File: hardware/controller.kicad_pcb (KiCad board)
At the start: 4 copper layers, 31.2 x 93.2 mm, 42 parts, among them J1 Connector, USB-TYPE-C-16P, J2 AXK6F20347YG, J3 AFA01-S08FCA-00, U1 ESP32-C6-WROOM-1, U2 BQ24074RGTR, U3 TLA2518IRTER, U6 TPS62142RGTR

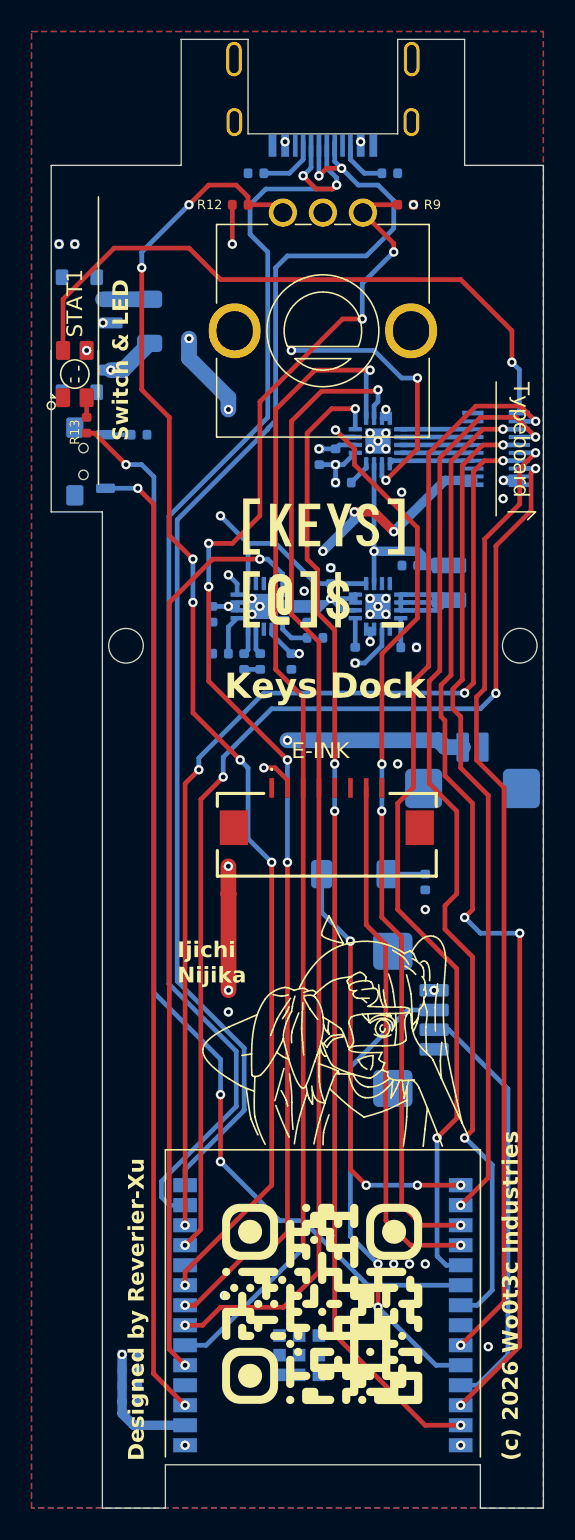
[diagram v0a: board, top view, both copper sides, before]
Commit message: :art: improve LED positions
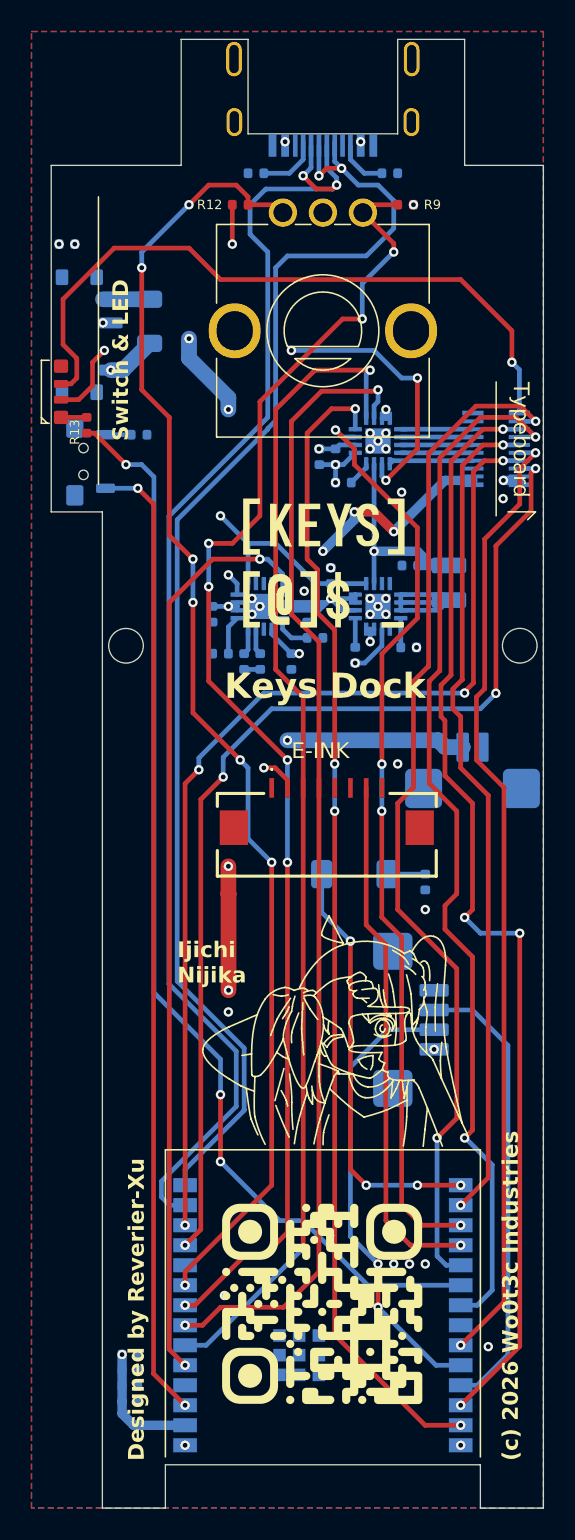
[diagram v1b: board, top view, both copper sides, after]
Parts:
- removed STAT1: ~, KeysDock:XL-3528RGBW-WS2812B
- added LED1: ~, KeysDock:XL-3512RGBW-WS2812B, F.Cu at (132.0, 68.1)
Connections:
- PC1 pad 1: P,E -> /USB_PWR_SUPP
- PC1 pad 2: /U0TX -> /U0RX
- PC1 pad 3: /U0RX -> /U0TX
- PC1 pad 4: /USB_PWR_SUPP -> P,E
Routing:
- net P,+5: track 61.5 -> 65.3 mm
- net /TOMO0: track 40.7 -> 44.0 mm
- net /U0TX: track 26.9 -> 29.1 mm
- net /USB_PWR_SUPP: track 84.6 -> 86.1 mm
- net /U0RX: track 29.6 -> 29.0 mm
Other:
- board text added: "-0 TX RX +5"
- board text removed: "+5 RX TX -0"
